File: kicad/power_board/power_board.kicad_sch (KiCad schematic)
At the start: 0 parts

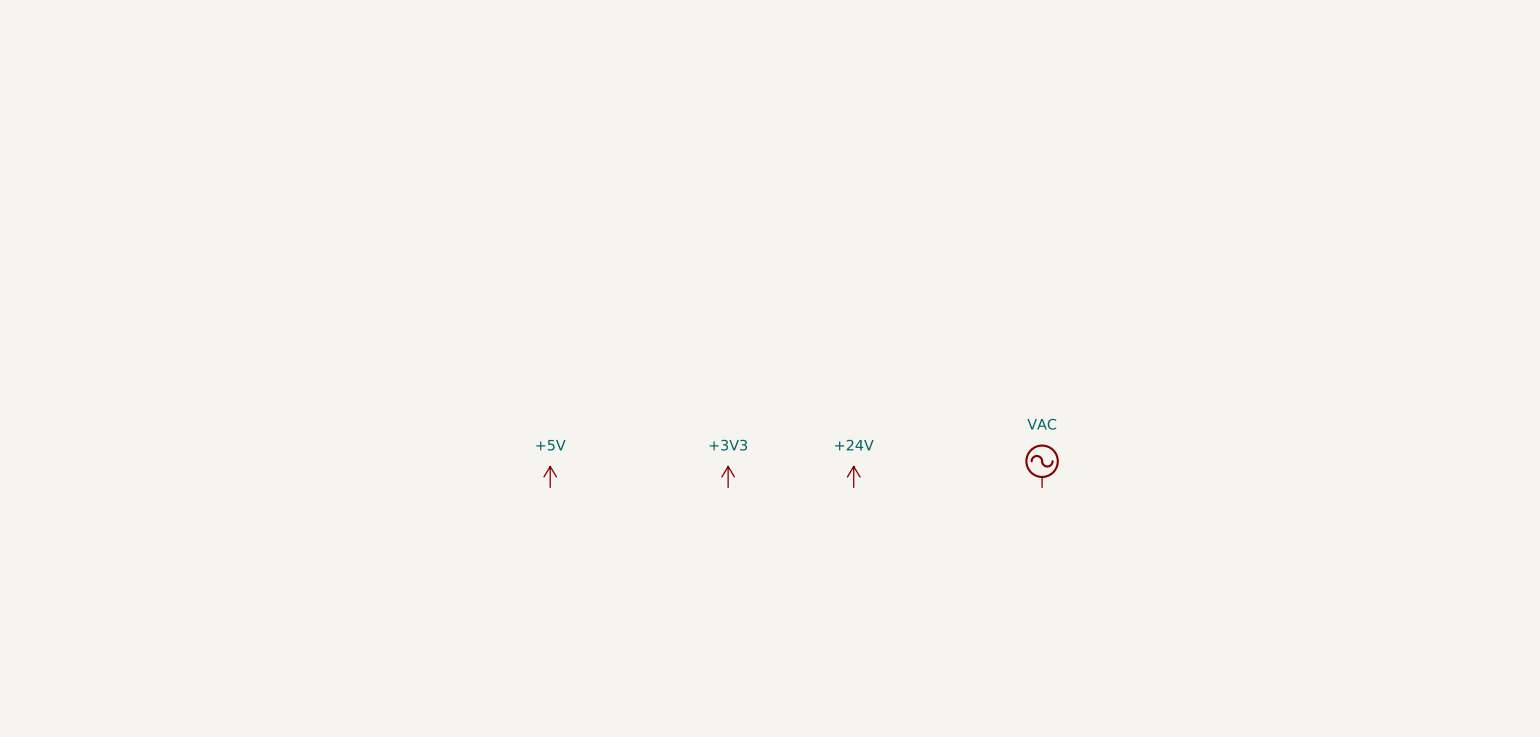
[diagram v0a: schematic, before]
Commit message: removed backups, added buck converters
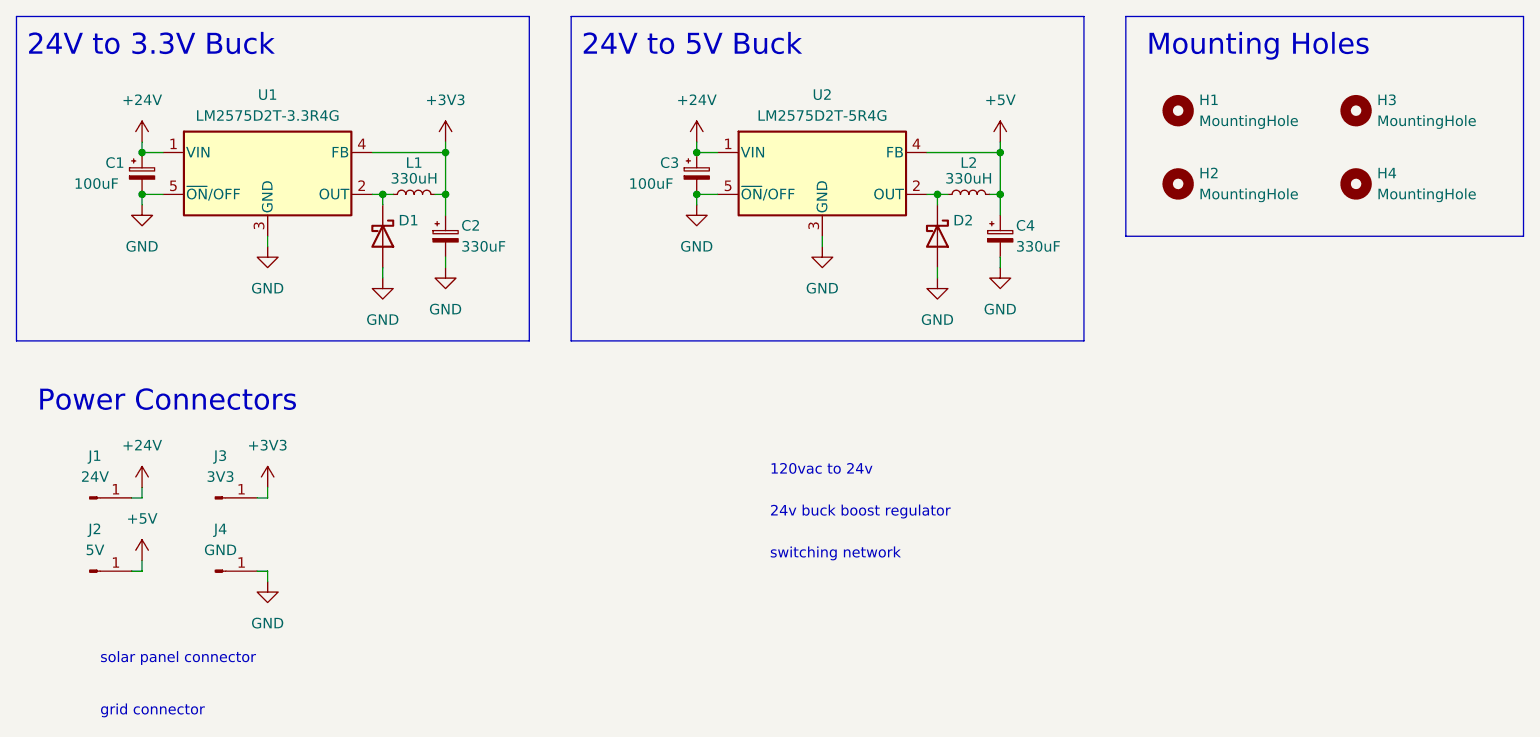
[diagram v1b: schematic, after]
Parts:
- added C1, C3: 100uF, symbol Device:C_Polarized_Small
- added C2, C4: 330uF, symbol Device:C_Polarized_Small
- added D1, D2: VS-30WQ04FNTR-M3, symbol Device:D_Schottky
- added H1, H2, H3, H4: MountingHole, symbol Mechanical:MountingHole
- added J1: 24V, symbol Connector:Conn_01x01_Male
- added J2: 5V, symbol Connector:Conn_01x01_Male
- added J3: 3V3, symbol Connector:Conn_01x01_Male
- added J4: GND, symbol Connector:Conn_01x01_Male
- added L1, L2: 330uH, symbol Device:L_Small
- added U1: LM2575D2T-3.3R4G, Package_TO_SOT_SMD:TO-263-5_TabPin3, symbol Regulator_Switching:LM2575-3.3BU
- added U2: LM2575D2T-5R4G, Package_TO_SOT_SMD:TO-263-5_TabPin3, symbol Regulator_Switching:LM2575-5.0BU
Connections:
- net +24V: now also C1.1, C3.1, J1.1 (Pin_1), U1.1 (VIN), U2.1 (VIN)
- net +3V3: now also C2.1, J3.1 (Pin_1), L1.2, U1.4 (FB)
- net +5V: now also C4.1, J2.1 (Pin_1), L2.2, U2.4 (FB)
- new net: D2.1 (K), L2.1, U2.2 (OUT)
- new net: D1.1 (K), L1.1, U1.2 (OUT)
- new net GND: C1.2, C2.2, C3.2, C4.2, D1.2 (A), D2.2 (A), J4.1 (Pin_1), U1.3 (GND), U1.5 (~{ON}/OFF), U2.3 (GND), U2.5 (~{ON}/OFF)
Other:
- note added: "120vac to 24v"
- note added: "24V to 3.3V Buck"
- note added: "24V to 5V Buck"
- note added: "24v buck boost regulator"
- note added: "Mounting Holes"
- note added: "Power Connectors"
- note added: "grid connector"
- note added: "solar panel connector"
- note added: "switching network"

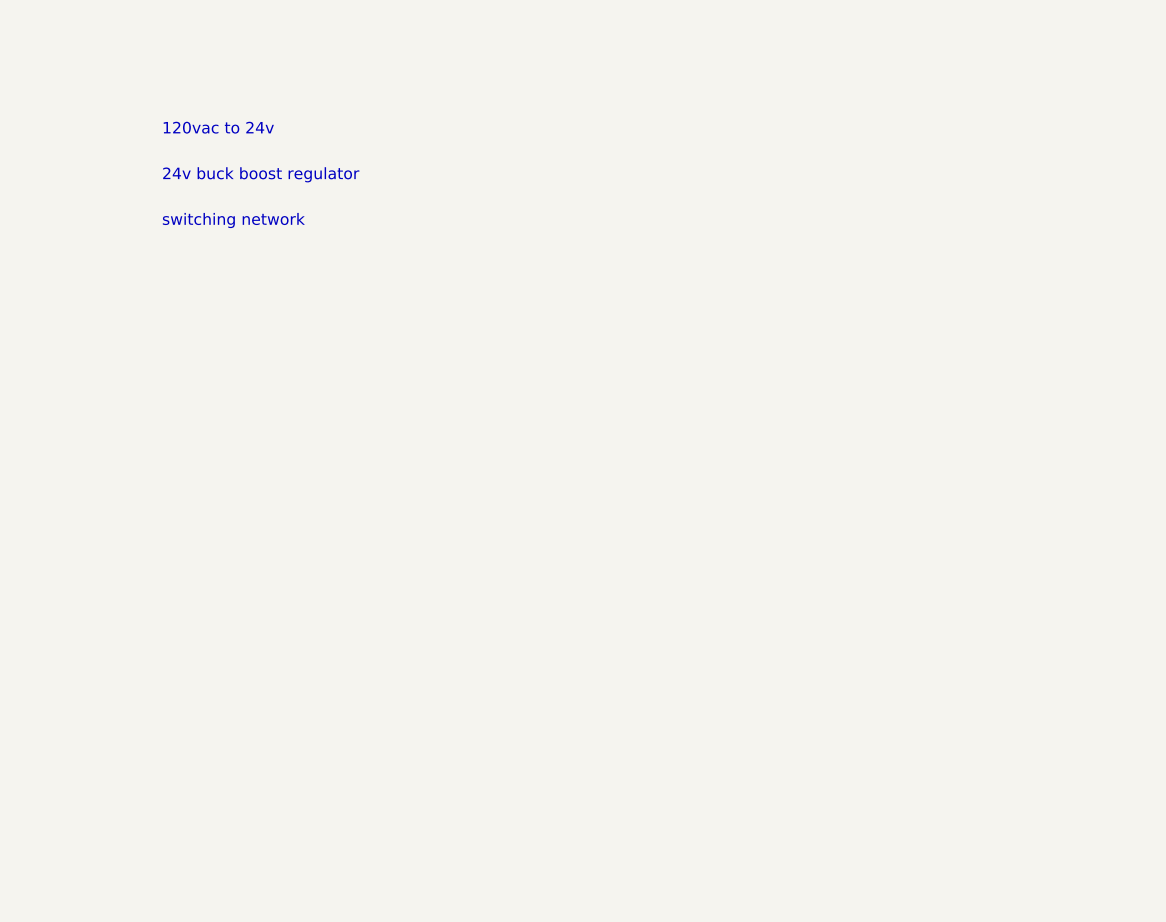
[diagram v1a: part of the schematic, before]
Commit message: added ltc4359 ckt + components
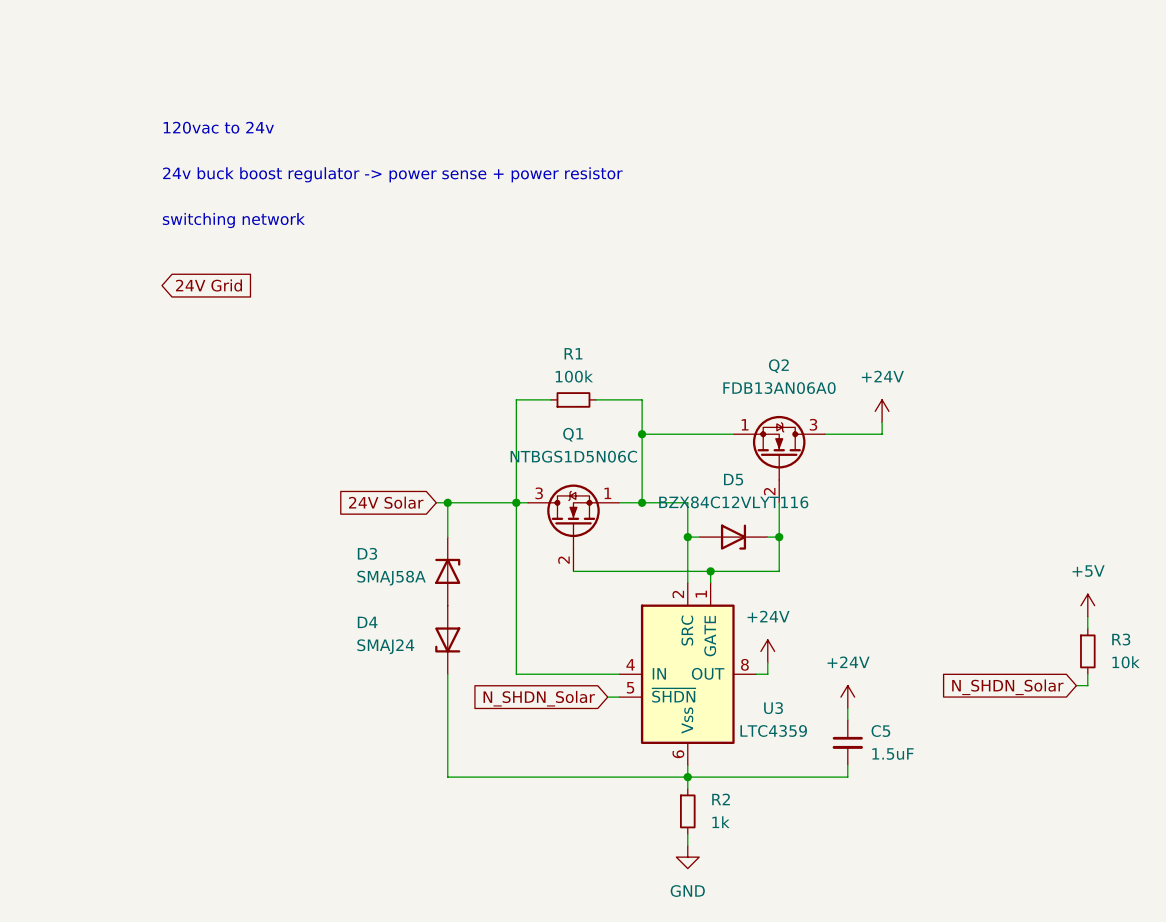
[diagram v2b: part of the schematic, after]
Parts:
- added C5: 1.5uF, symbol Device:C_Small
- added D3: SMAJ58A, symbol Device:D_Zener
- added D4: SMAJ24, symbol Device:D_Zener
- added D5: BZX84C12VLYT116, symbol Device:D_Zener
- added Q1: NTBGS1D5N06C, Package_TO_SOT_THT:TO-92_Inline, symbol Transistor_FET:2N7000
- added Q2: FDB13AN06A0, Package_TO_SOT_THT:TO-92_Inline, symbol Transistor_FET:2N7000
- added R1: 100k, symbol Device:R_Small
- added R2: 1k, symbol Device:R_Small
- added R3: 10k, symbol Device:R_Small
- added U3: LTC4359, Package_SO:MSOP-8_3x3mm_P0.65mm, symbol Power_Management:LTC4359-MS8
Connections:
- net +24V: now also C5.1, Q2.3 (D), U3.8 (OUT)
- net +5V: now also R3.1
- net GND: now also R2.2
- new net: D5.2 (A), Q1.1 (S), Q2.1 (S), R1.2, U3.2 (SRC)
- new net: D5.1 (K), Q1.2 (G), Q2.2 (G), U3.1 (GATE)
- new net: D3.2 (A), D4.2 (A)
- new net: C5.2, D4.1 (K), R2.1, U3.6 (Vss)
- new net 24V Solar: D3.1 (K), Q1.3 (D), R1.1, U3.4 (IN)
- new net N_SHDN_Solar: R3.2, U3.5 (~{SHDN})
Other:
- note added: "24v buck boost regulator -> power sense + power resistor"
- note removed: "24v buck boost regulator"

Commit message: add simulations
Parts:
- added C6: 1.5uF, symbol Device:C_Small
- added D6: SMAJ58A, symbol Device:D_Zener
- added D7: SMAJ24, symbol Device:D_Zener
- added D8: BZX84C12VLYT116, symbol Device:D_Zener
- added Q3: NTBGS1D5N06C, Package_TO_SOT_THT:TO-92_Inline, symbol Transistor_FET:2N7000
- added Q4: FDB13AN06A0, Package_TO_SOT_THT:TO-92_Inline, symbol Transistor_FET:2N7000
- added R4: 100k, symbol Device:R_Small
- added R5: 1k, symbol Device:R_Small
- added R6: 10k, symbol Device:R_Small
- added U4: LTC4359, Package_SO:MSOP-8_3x3mm_P0.65mm, symbol Power_Management:LTC4359-MS8
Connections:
- net +24V: now also C6.1, Q4.3 (D), U4.8 (OUT)
- net +5V: now also R6.1
- net 24V Grid: now also D6.1 (K), Q3.3 (D), R4.1, U4.4 (IN)
- net GND: now also R5.2
- new net: D8.2 (A), Q3.1 (S), Q4.1 (S), R4.2, U4.2 (SRC)
- new net: D8.1 (K), Q3.2 (G), Q4.2 (G), U4.1 (GATE)
- new net: C6.2, D7.1 (K), R5.1, U4.6 (Vss)
- new net: D6.2 (A), D7.2 (A)
- new net N_SHDN_Grid: R6.2, U4.5 (~{SHDN})
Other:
- note added: "Switching Network"
- note removed: "switching network"
- moved on the sheet: C5, D3, D4, D5, Q1, Q2, R1, R2, R3, U3
